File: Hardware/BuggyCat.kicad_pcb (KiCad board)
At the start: 2 copper layers, 51.2 x 124.2 mm, 105 parts, among them J1 Antenna, J2 BG306-02-A-2-0400-L-G, J3 Header7, J4 Header 2, J5 Header 4, J6 Input Power:2x AA Battery, P1 USB_C_Plug_USB2.0, Q1 AO3422, Q2 AO3422, Q3 LDA111STR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

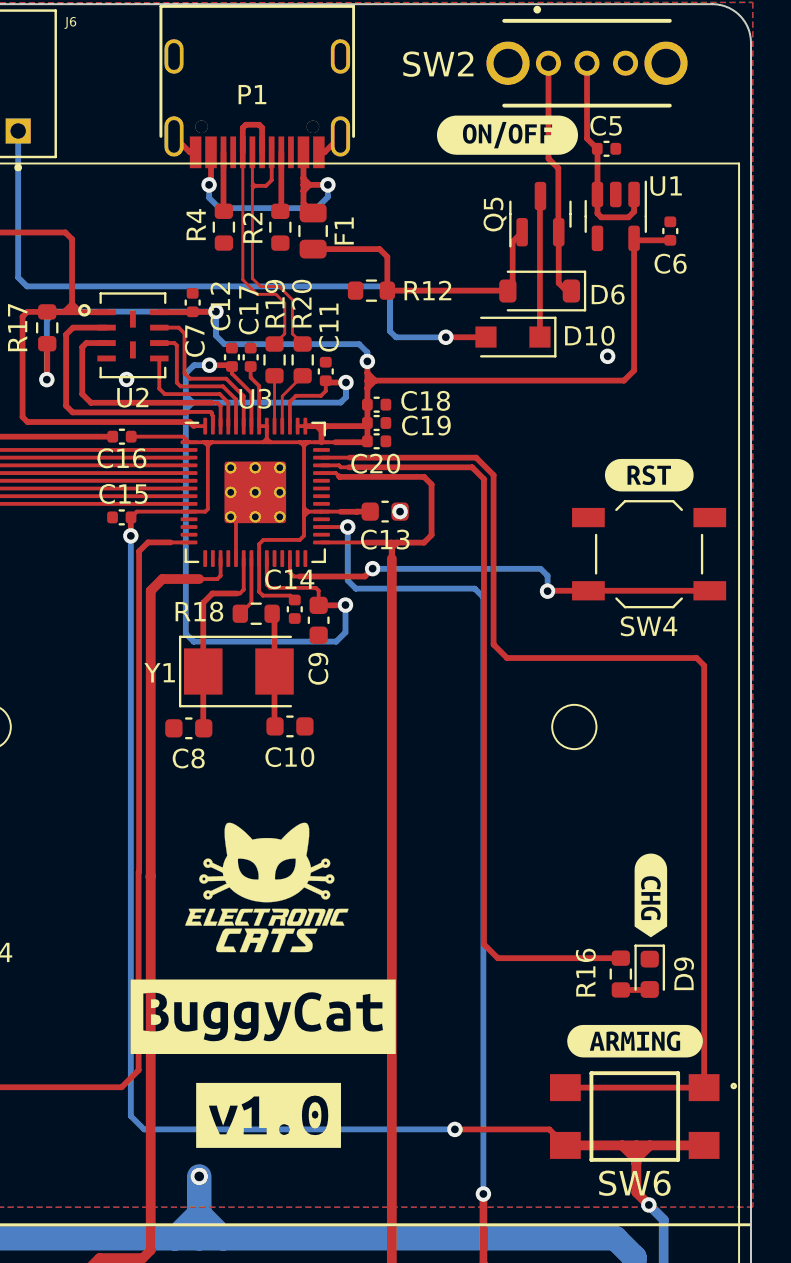
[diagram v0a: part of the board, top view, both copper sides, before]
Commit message: Change name and logos
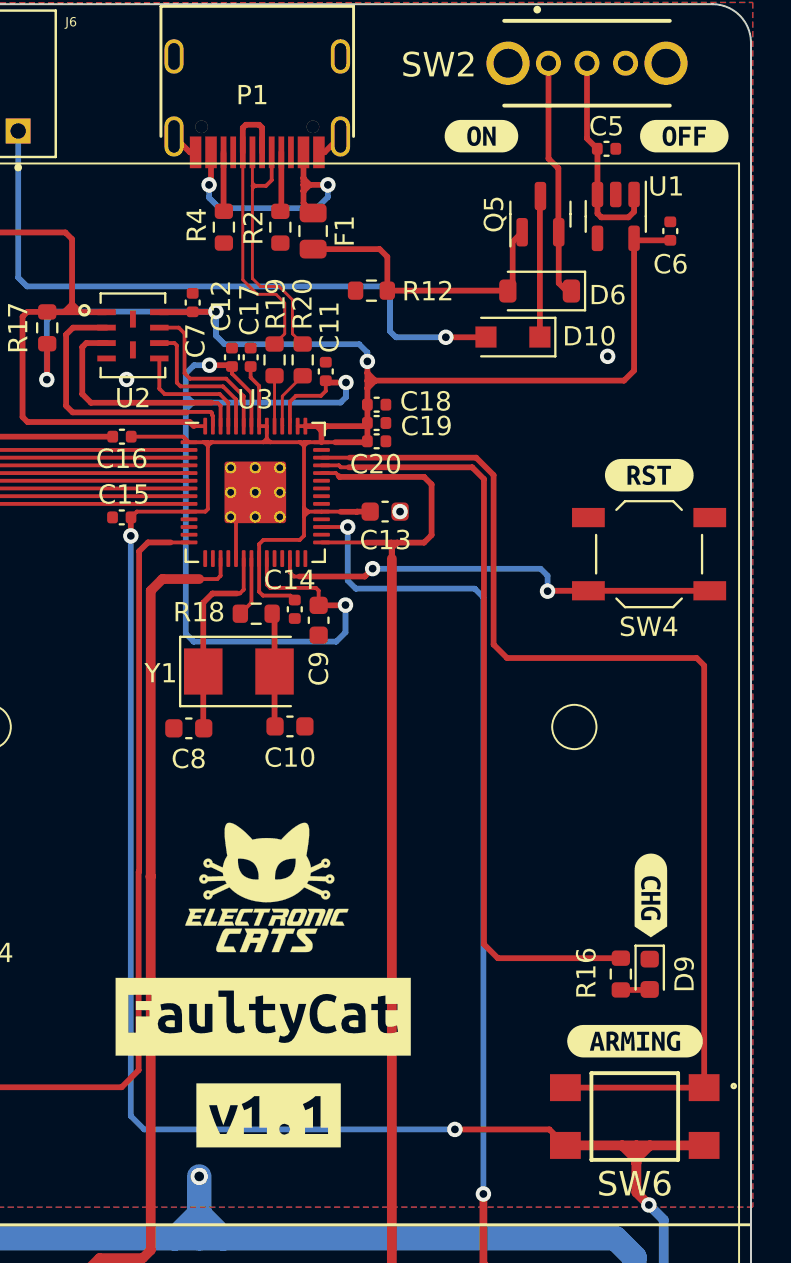
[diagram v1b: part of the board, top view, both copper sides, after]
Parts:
- removed kibuzzard-642DF8F6: G***, kibuzzard-642DF8F6
- removed kibuzzard-642E0E1B: G***, kibuzzard-642E0E1B
- removed kibuzzard-642E0E2F: G***, kibuzzard-642E0E2F
- added kibuzzard-6475468D: G***, kibuzzard-6475468D, F.Cu at (110.9, 77.9)
- added kibuzzard-647546A8: G***, kibuzzard-647546A8, F.Cu at (122.2, 32.2)
- added kibuzzard-647546B9: G***, kibuzzard-647546B9, F.Cu at (132.8, 32.2)
- added kibuzzard-647546C2: G***, kibuzzard-647546C2, F.Cu at (111.2, 83.0)
- moved REF** 21.6 mm to (110.5, 132.0)
